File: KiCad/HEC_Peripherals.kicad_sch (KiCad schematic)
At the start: 23 parts, among them J2 Conn_02x12_Odd_Even, J6 DE9_Plug_MountingHoles, J7 AudioJack3, J8 NES_Port_Male, J9 Conn_02x05_Odd_Even, U43 74LS06, U44 74LS541, U47 TL074, Y1 Crystal

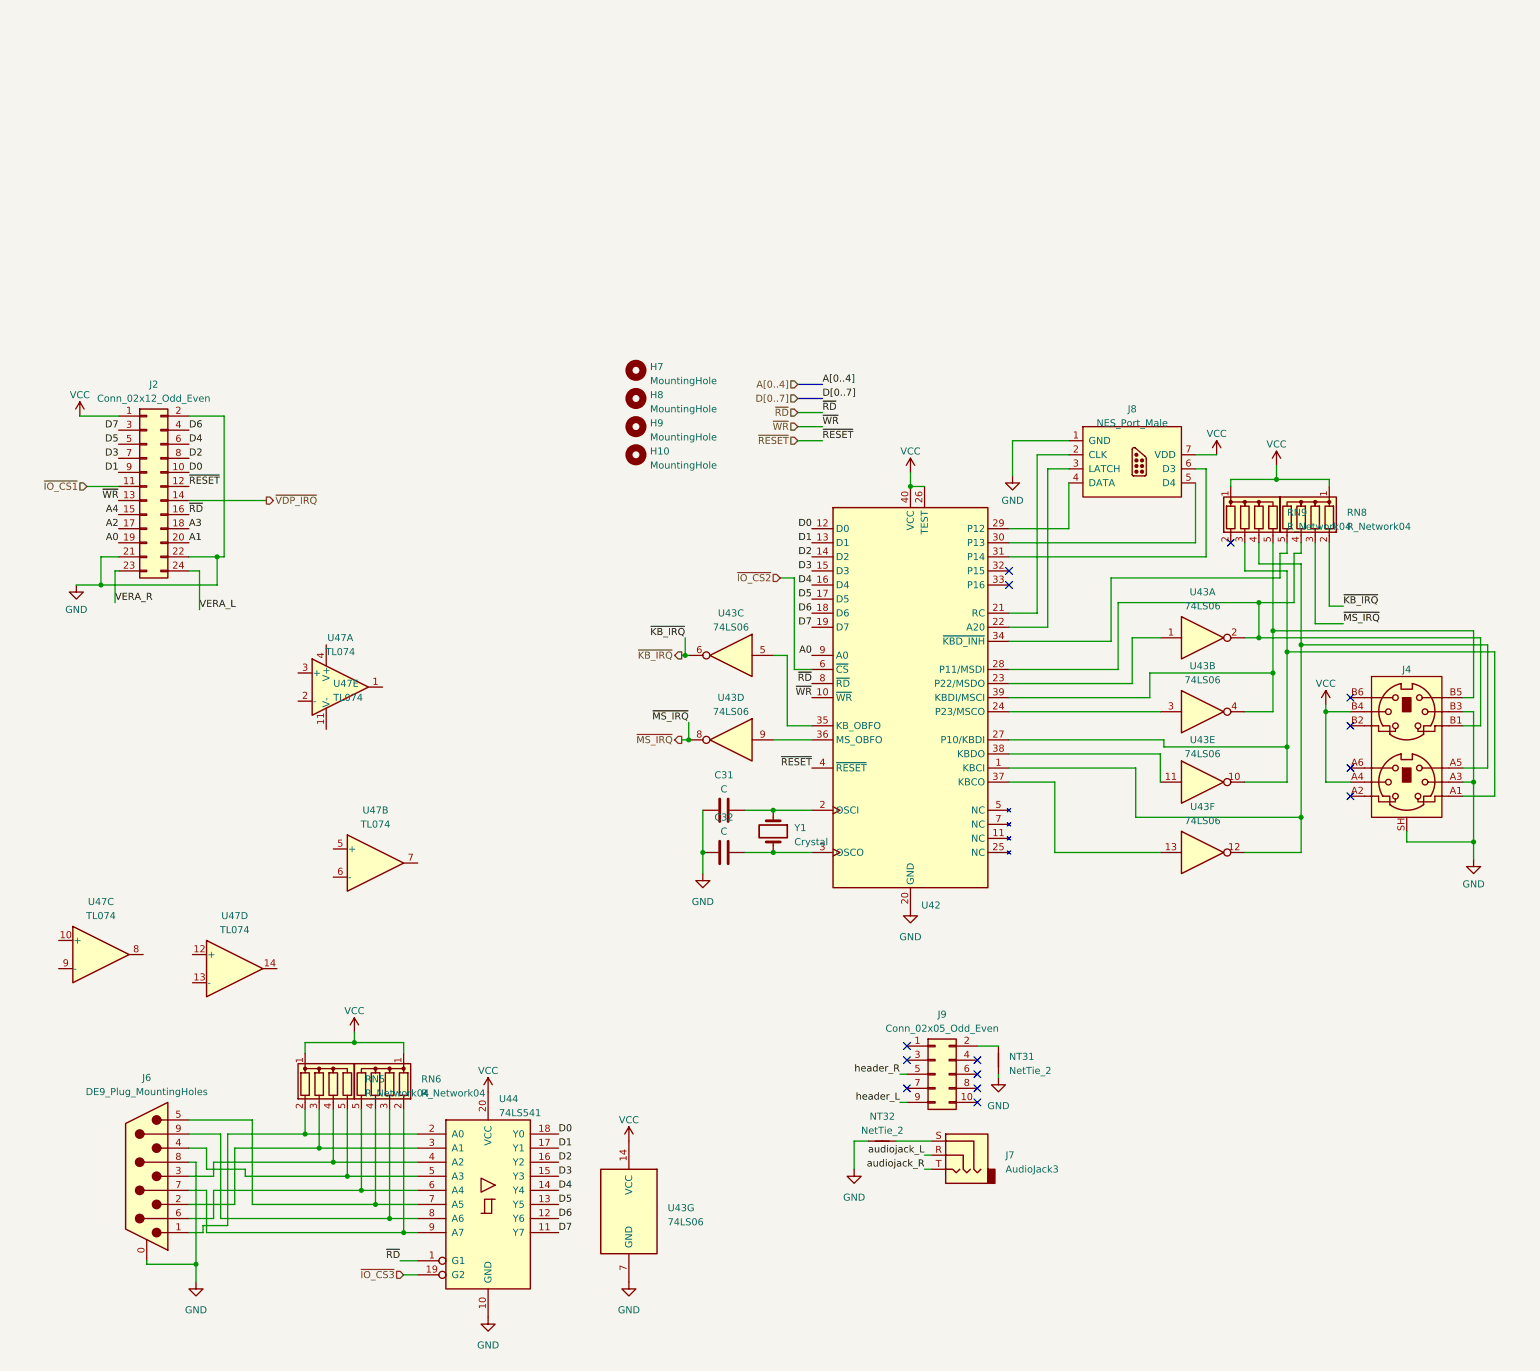
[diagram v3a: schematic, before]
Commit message: Updates to schematic
Unfinished design of V2 schematic
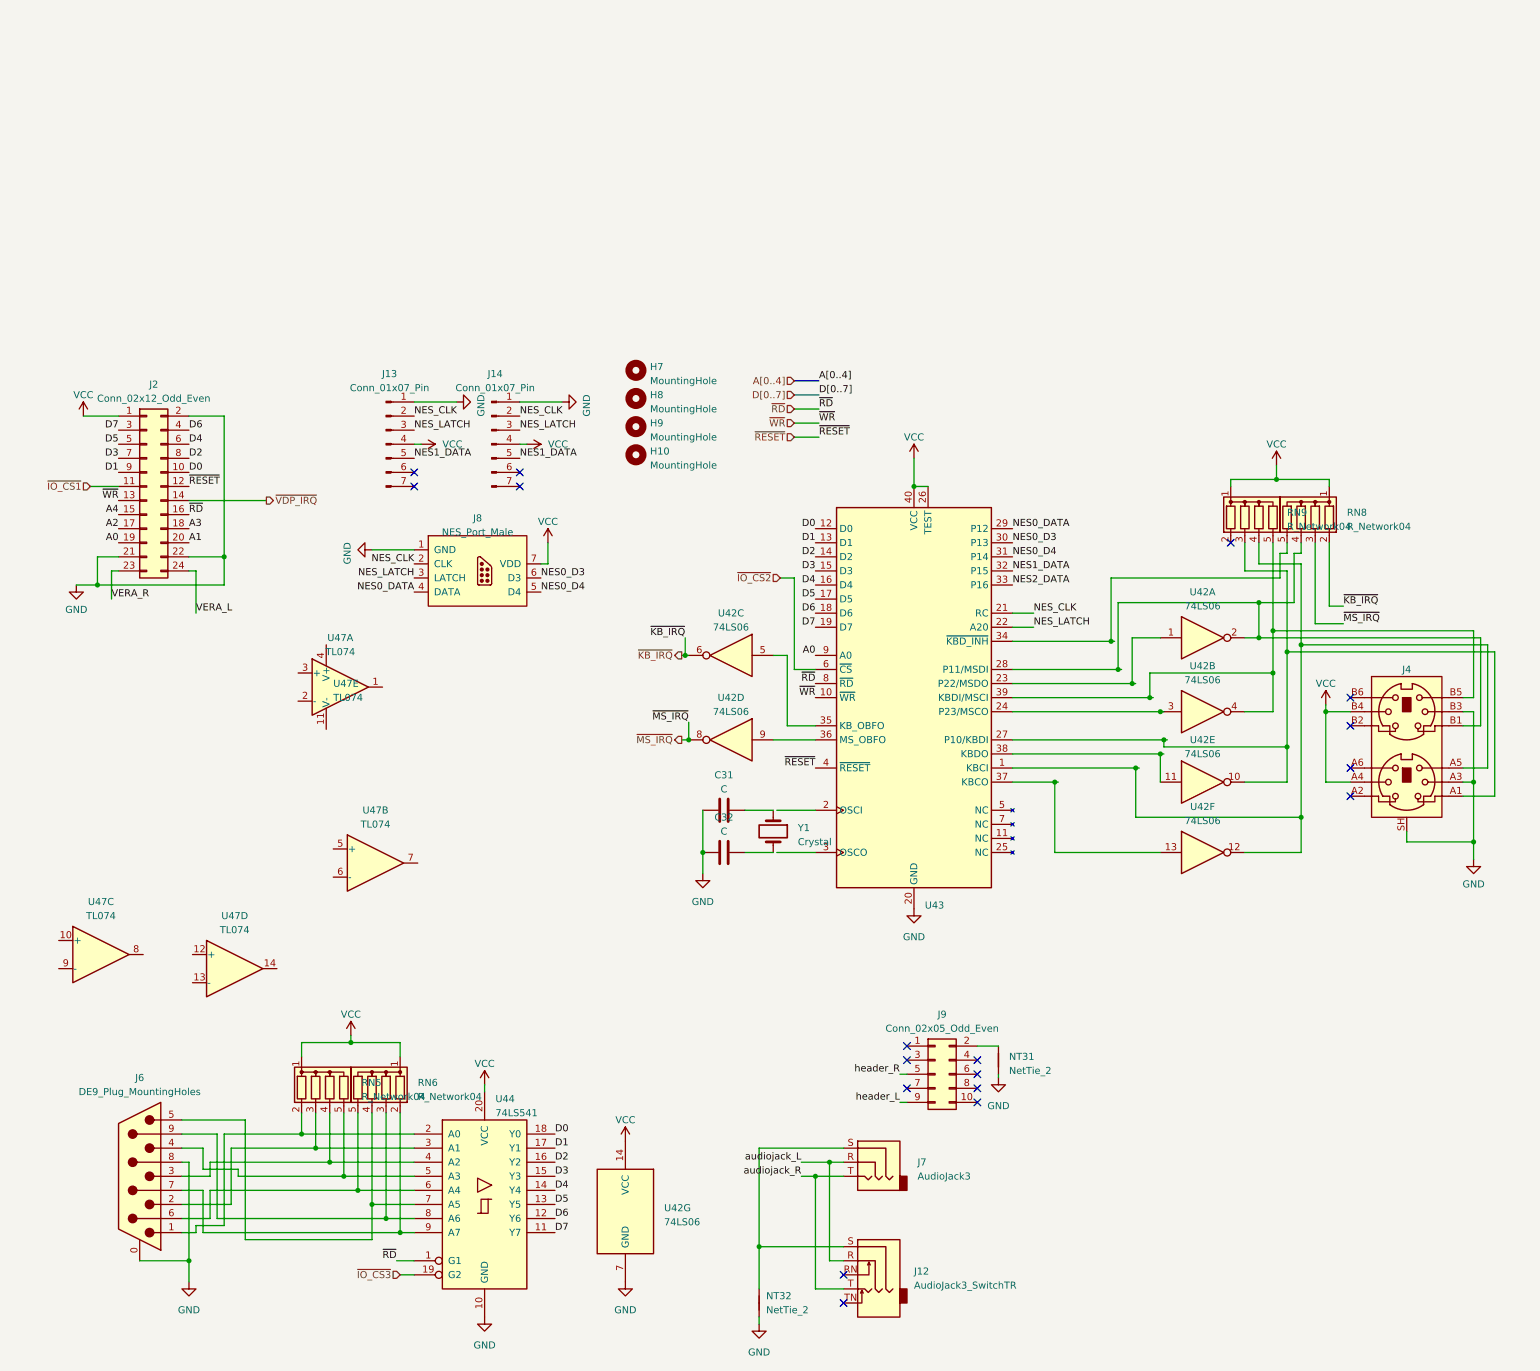
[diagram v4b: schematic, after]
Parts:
- added J12: AudioJack3_SwitchTR, Connector_Audio:Jack_3.5mm_CUI_SJ1-3525N_Horizontal, symbol Connector_Audio:AudioJack3_SwitchTR
- added J13, J14: Conn_01x07_Pin, Connector_JST:JST_PH_B7B-PH-K_1x07_P2.00mm_Vertical, symbol Connector:Conn_01x07_Pin
- J9: footprint (none) -> Connector_PinHeader_2.54mm:PinHeader_2x05_P2.54mm_Vertical
- NT31, NT32: footprint (none) -> NetTie:NetTie-2_SMD_Pad0.5mm
- U47: footprint (none) -> Package_DIP:DIP-14_W7.62mm_Socket
- renumbered U43 to U42, U42 to U43
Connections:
- net GND: now also J13.1 (Pin_1), J14.1 (Pin_1)
- net VCC: now also J13.4 (Pin_4), J14.4 (Pin_4)
- net audiojack_L: now also J12.R
- net audiojack_R: now also J12.T
- net at C31.2, Y1.1: no longer U43.2 (OSCI)
- net at J7.S, NT32.2: now also J12.S
- net at C32.2, Y1.2: no longer U43.3 (OSCO)
- net NES_CLK: now reaches J8.2 (CLK), U43.21 (RC)
- net NES_CLK: now also J13.2 (Pin_2), J14.2 (Pin_2)
- net NES_LATCH: now reaches J8.3 (LATCH), U43.22 (A20)
- net NES_LATCH: now also J13.3 (Pin_3), J14.3 (Pin_3)
- net NES0_DATA: now reaches J8.4 (DATA), U43.29 (P12)
- net NES0_D3: now reaches U43.30 (P13)
- net NES0_D3: now also J8.6 (D3); no longer J8.5 (D4)
- net NES0_D4: now reaches U43.31 (P14)
- net NES0_D4: now also J8.5 (D4); no longer J8.6 (D3)
- net NES1_DATA: now reaches U43.32 (P15)
- net NES1_DATA: now also J13.5 (Pin_5), J14.5 (Pin_5)
- net NES2_DATA: now reaches U43.33 (P16)
- no-connect marks 14 -> 18
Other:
- moved on the sheet: J6, J7, J8, NT32, RN5, RN6, U42G, U43, U44

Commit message: Update to KiCad 8.0, clean up schematic
Cleaned up the IO schematic using experience from model 9 schematic. Changed the controller pinout to be compatible with the Kempston standard.
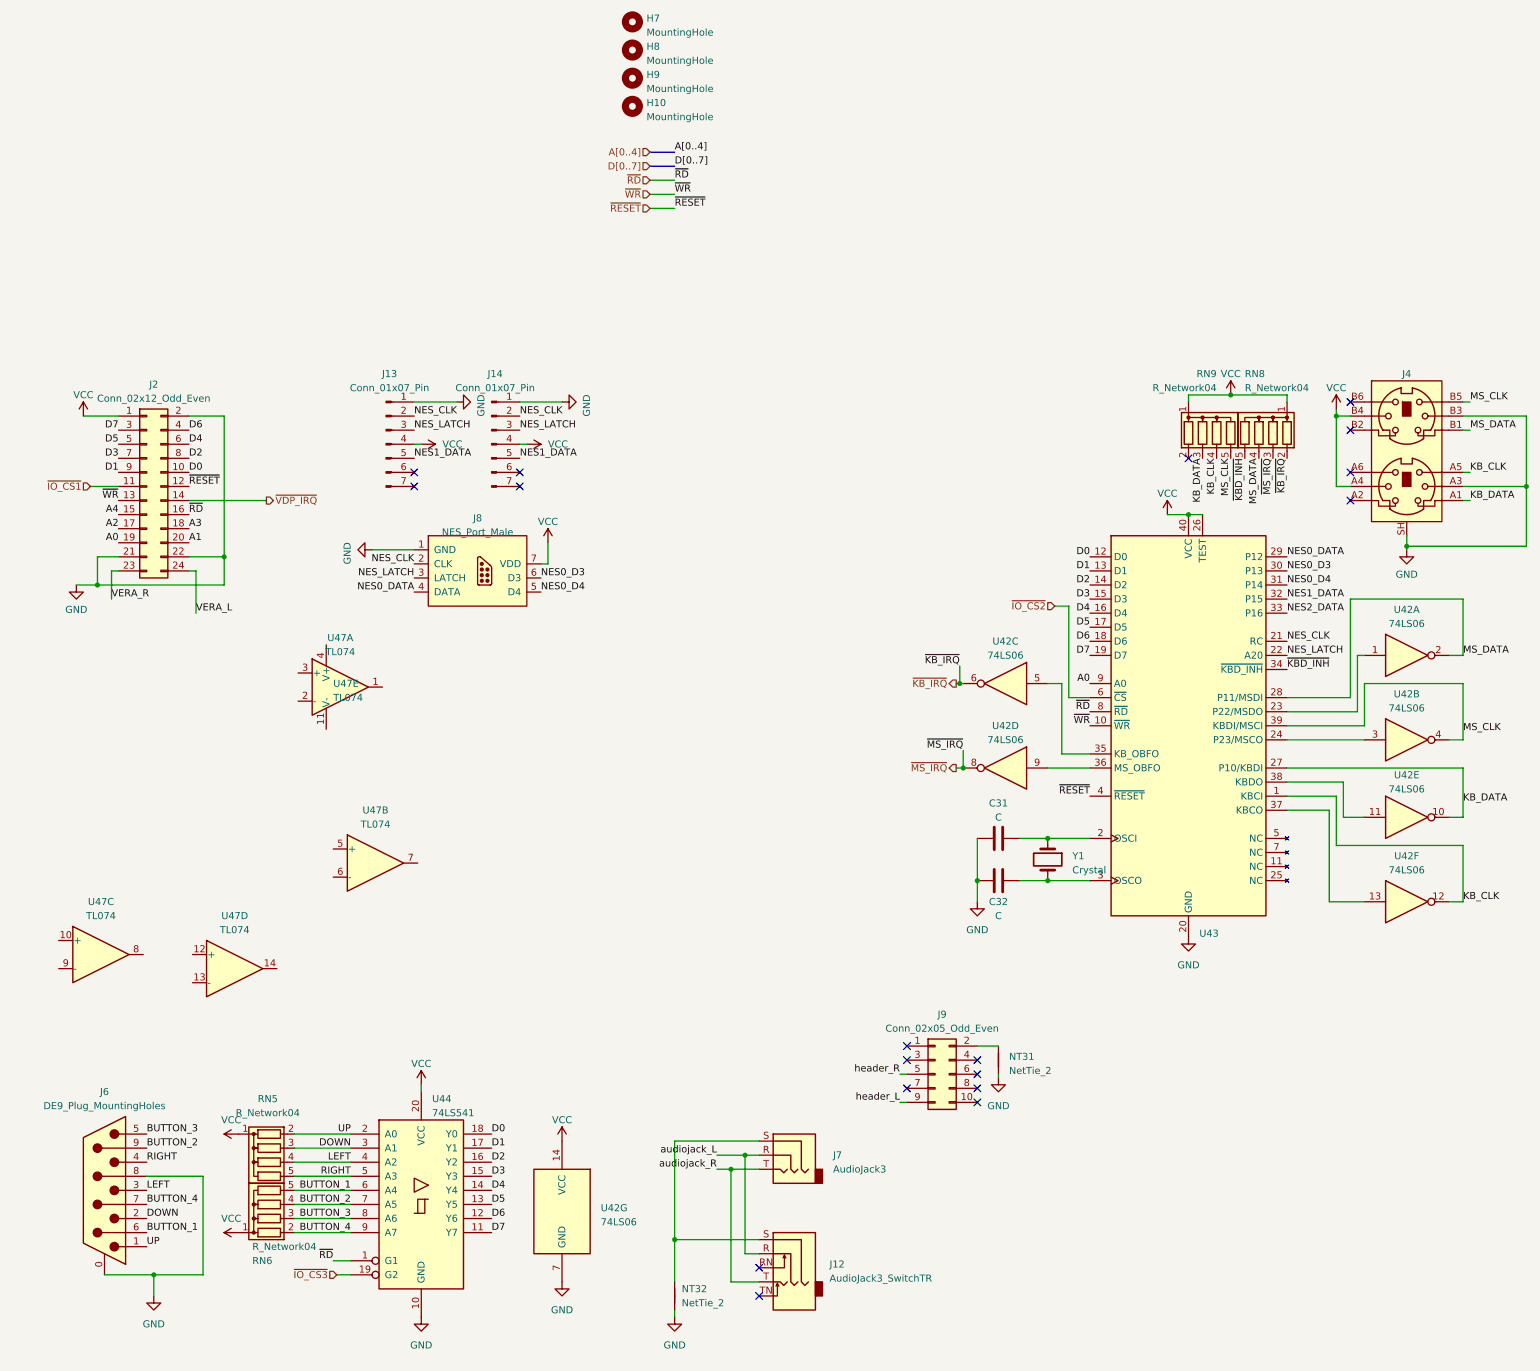
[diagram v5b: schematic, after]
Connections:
- net KB_DATA: now reaches J4.A1, RN9.3 (R2), U42.10, U43.27 (P10/KBDI)
- net KB_CLK: now reaches J4.A5, RN9.4 (R3), U42.12, U43.1 (KBCI)
- net MS_DATA: now reaches J4.B1, RN8.4 (R3), U42.2, U43.28 (P11/MSDI)
- net MS_CLK: now reaches J4.B5, RN9.5 (R4), U42.4, U43.39 (KBDI/MSCI)
- net at C31.2, Y1.1: now also U43.2 (OSCI)
- net UP: now reaches J6.1, RN5.2 (R1), U44.2 (A0)
- net DOWN: now reaches J6.2, RN5.3 (R2), U44.3 (A1)
- net LEFT: now reaches J6.3, RN5.4 (R3), U44.4 (A2)
- net RIGHT: now reaches J6.4, RN5.5 (R4), U44.5 (A3)
- net ~{KBD_INH}: now reaches RN8.5 (R4), U43.34 (~{KBD_INH})
- net at C32.2, Y1.2: now also U43.3 (OSCO)
- net BUTTON_1: now reaches J6.6, RN6.5 (R4), U44.6 (A4)
- net BUTTON_2: now reaches RN6.4 (R3), U44.7 (A5)
- net BUTTON_2: now also J6.9; no longer J6.5
- net BUTTON_3: now reaches RN6.3 (R2), U44.8 (A6)
- net BUTTON_3: now also J6.5; no longer J6.9
- net BUTTON_4: now reaches J6.7, RN6.2 (R1), U44.9 (A7)
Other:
- moved on the sheet: C31, C32, H10, H7, H8, H9, J12, J4, J6, J7, NT32, RN5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

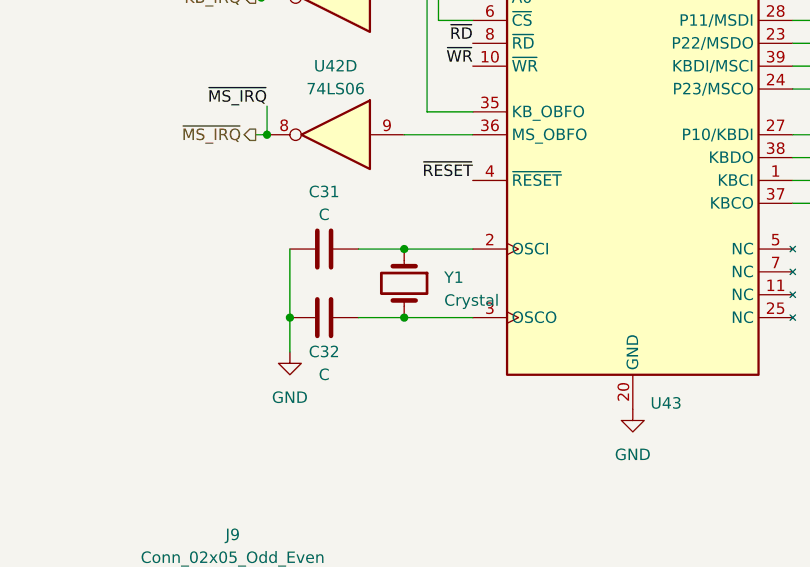
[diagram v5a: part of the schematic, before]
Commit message: Completed i2c subsystem
Updates to schematic, the i2c driver is circuit now complete.
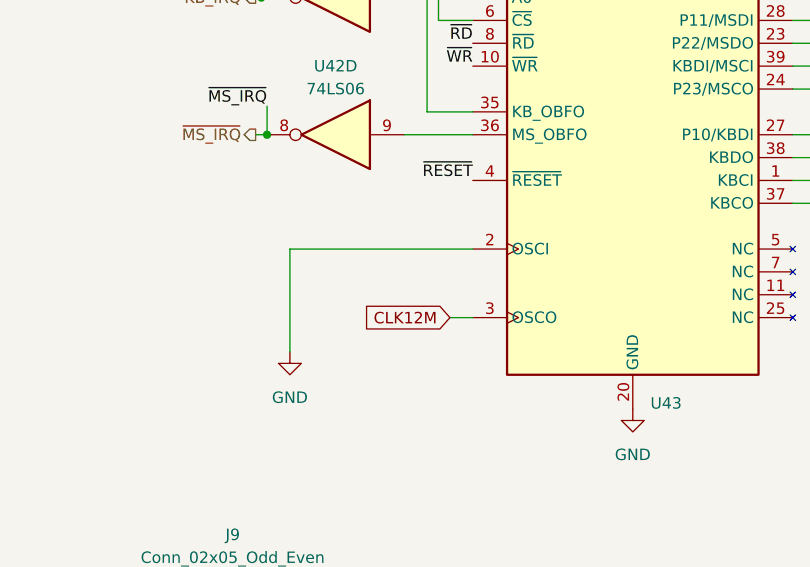
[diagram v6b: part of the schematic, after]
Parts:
- removed C31, C32: C, Capacitor_THT:C_Disc_D3.4mm_W2.1mm_P2.50mm, symbol Device:C
- removed Y1: Crystal, Crystal:Crystal_HC18-U_Vertical, symbol Device:Crystal
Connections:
- net GND: now also U43.2 (OSCI)
- net CLK12M: now reaches U43.3 (OSCO)
